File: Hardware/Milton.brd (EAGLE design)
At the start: 53 x 44.8 mm, 83 parts, among them Q1 12MHz, U1 FT231X, U10 SI4464, U3 USD-SOCKETNEW, U4 DDC113TU-7-F, U5 TPS61200, U6 TCR2EE50,LM, U7 MMA8452Q, U8 MAX31850K, U9 BME280, X1 B4B-ZR, X2 M023.5MM, X3 SMA003.062

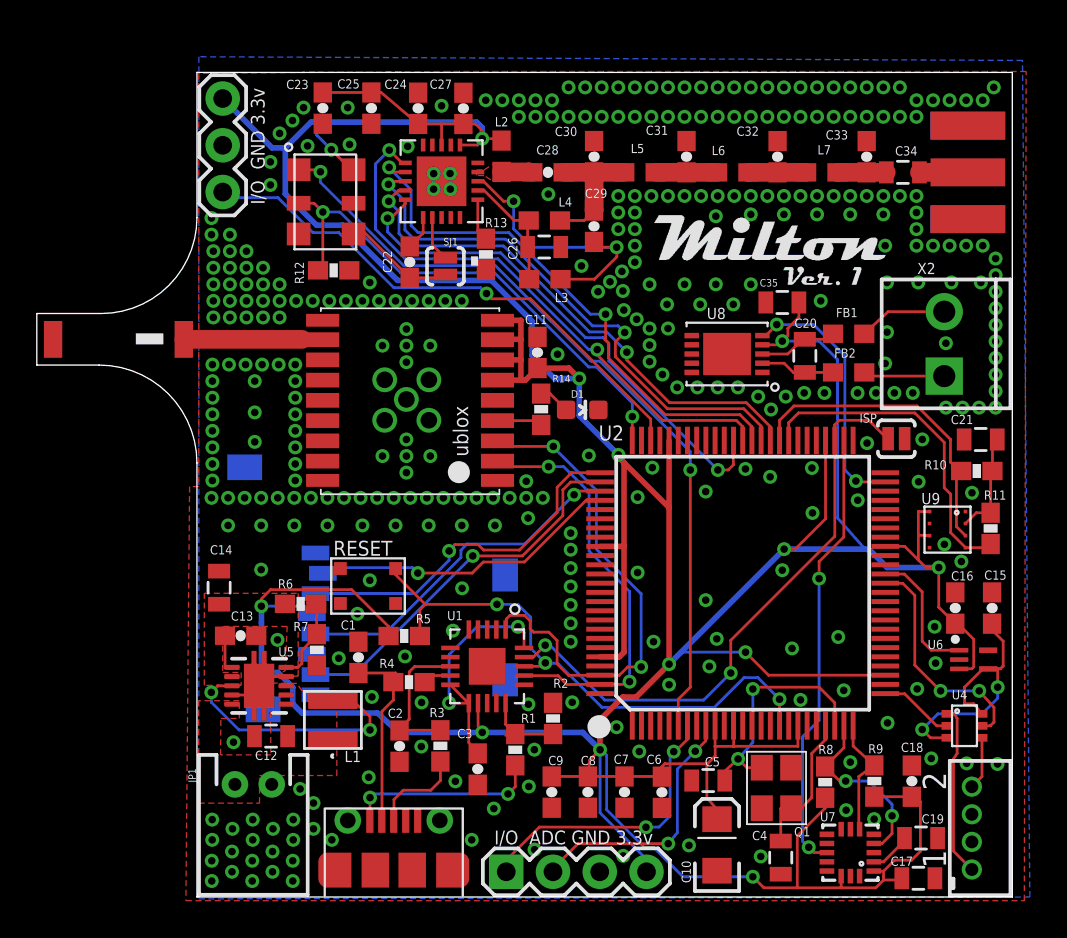
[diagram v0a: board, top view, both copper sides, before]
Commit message: Update
Removed FTDI from board. Added tx/rx header and isp button

Adjusted gps antenna position
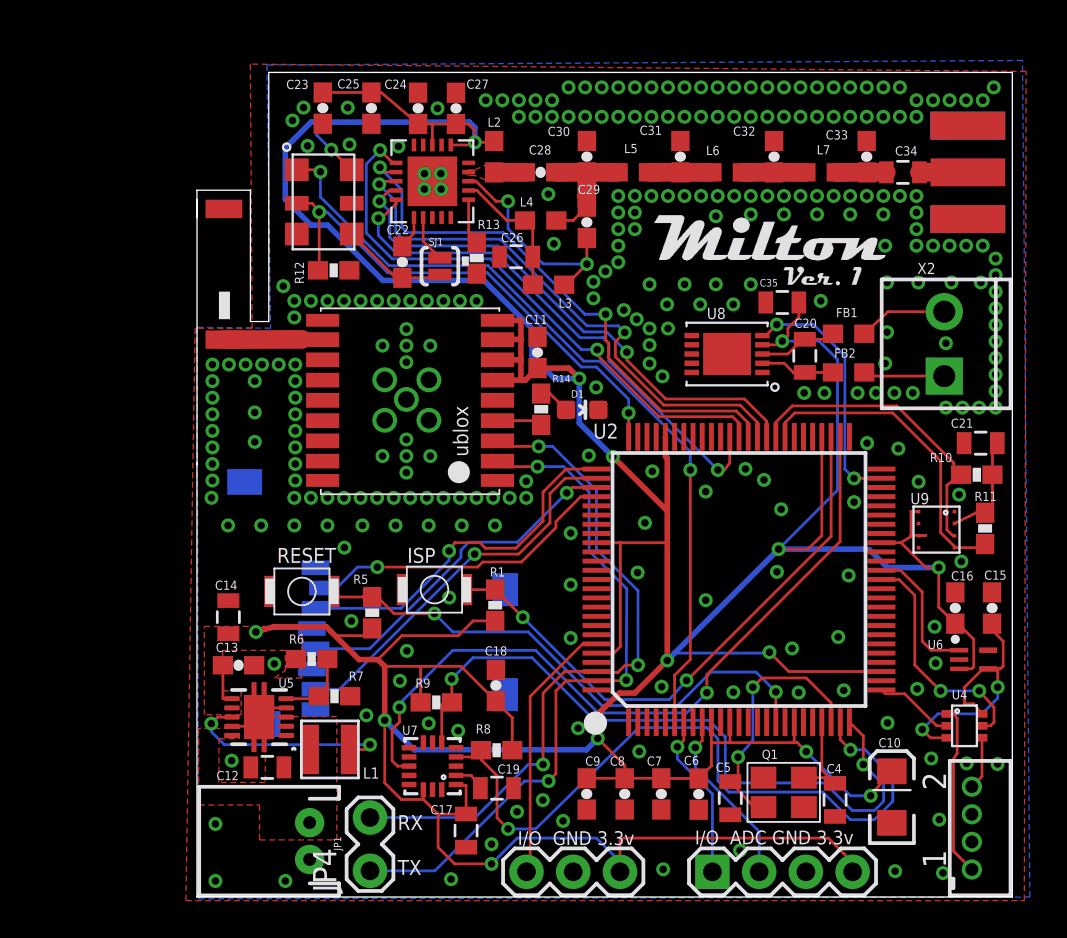
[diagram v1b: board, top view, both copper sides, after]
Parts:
- removed C1, C2: 47pF, SparkFun-Capacitors:0603-CAP
- removed C3: 0.1uF, SparkFun-Capacitors:0603-CAP
- removed R2: 10k, SparkFun-Resistors:0603-RES
- removed R3, R4: 27, SparkFun-Resistors:0603-RES
- removed U$1: USB-MICRO_105017-0001, wrea:USB-MICRO-MOLEX-105017-0001
- removed U1: FT231X, wrea:FT231XQ-R
- added JP4: (no value), SparkFun-Connectors:1X02_LOCK
- ISP: value JUMPER-PAD-2-NOYES_SILK -> SPST.B3U-1000P(M); device SparkFun-Passives:PAD-JUMPER-2-NO_YES_SILK -> omron:B3U-1000P(M)
- JP1: value M02JST-PTH-2 -> (none)
- R1: value 4.7k -> 10K
- RESET: value SWITCH -> SPST.B3U-1000P(M); device notes-arducorder-mini:KMT071 -> omron:B3U-1000P(M)
- moved JP2 40.4 mm to (17.9, 1.37), turned to 0 degrees
- moved ISP 26.4 mm to (12.9, 16.7), turned to 0 degrees
- moved C17 24.7 mm to (14.6, 3.61), turned to 270 degrees
- moved R9 24.2 mm to (13.0, 10.6), turned to 180 degrees
- moved C19 23.2 mm to (16.3, 5.91)
- moved C18 23.2 mm to (16.2, 11.5)
- moved U7 23.2 mm to (12.8, 7.11)
- moved R8 17.9 mm to (16.3, 7.97), turned to 0 degrees
- moved JP3 11.2 mm to (28.0, 1.37)
- moved C10 9.85 mm to (37.8, 5.43)
- moved R1 7.93 mm to (16.2, 15.8)
- moved U$2 6.22 mm to (1.46, 33.5), turned to 90 degrees
- moved JP1 4.34 mm to (6.12, 3.04), turned to 90 degrees
- moved C4 4.30 mm to (34.7, 5.28)
- moved RESET 3.60 mm to (5.70, 16.6), turned to 0 degrees
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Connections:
- removed net N$10: R1.2, U$1.1
- removed net N$12: C3.1, U1.3V3OUT, U1.RESET#, U1.VCCIO
- removed net N$21: R1.1, R2.2, U1.CBUS0
- removed net N$4: C2.1, R3.2, U1.USBDP
- removed net N$5: R4.2, U1.USBDM
- removed net N$7: R3.1, U$1.3
- removed net N$9: C1.2, R4.1, U$1.2
- net 3.3V: now also R1.2; no longer U1.VCC
- net DIGITAL_1: now also U2.95; no longer U2.73
- net GND: now also RESET.1; no longer C1.1, C2.2, C3.2, R2.1, RESET.1A, U$1.5, U1.GND_PIN13, U1.GND_PIN21, U1.GND_PIN3
- net ISP_BOOT: now also R1.1; no longer U1.RTS#
- net RESET: now also RESET.2; no longer RESET.2A, U1.DTR#
- net RXD0: now also JP4.1; no longer U1.TXD
- net TXD0: now also JP4.2; no longer U1.RXD
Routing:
- net SDA0: track 6.57 -> 37.8 mm, vias 0 -> 2
- net SCL0: track 9.92 -> 39.5 mm
- net EINT1: track 24.3 -> 41.0 mm
- net DIGITAL_1: track 29.5 -> 14.4 mm, vias 1 -> 0
- net RXD0: track 23.0 -> 37.7 mm, vias 2 -> 3
- net N$12: track 13.7 -> 0.00 mm, vias 2 -> 0
- net N$9: track 11.2 -> 0.00 mm
- net N$10: track 10.5 -> 0.00 mm, vias 2 -> 0
- net TXD0: track 27.8 -> 37.3 mm, vias 2 -> 3
- net N$4: track 7.95 -> 0.00 mm
- net DIGITAL_2: track 15.9 -> 9.06 mm, vias 2 -> 1
- net N$7: track 5.13 -> 0.00 mm
- net 3.3V: track 290.3 -> 295.2 mm, vias 13 -> 15
- net ADC_IN1: track 14.2 -> 9.72 mm, vias 2 -> 1
- net N$21: track 4.48 -> 0.00 mm
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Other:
- board size 53 x 44.8 mm -> 44.3 x 44.8 mm
- board text added: "RX TX"

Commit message: Cleanup
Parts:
- added U$1: (no value), SparkFun-Aesthetics:OSHW-LOGO-S
- moved R1 4.54 mm to (12.2, 13.8), turned to 180 degrees
- moved L3 0.84 mm to (19.1, 34.1), turned to 270 degrees
- moved C26 0.75 mm to (17.2, 34.1), turned to 90 degrees
- moved ISP 0.70 mm to (12.2, 16.7)
- moved R9 0.67 mm to (13.2, 11.2), turned to 90 degrees
- moved D1 0.63 mm to (20.4, 26.2), turned to 180 degrees
- moved R5 0.60 mm to (8.92, 15.4)
- moved C18 0.51 mm to (16.1, 11.0)
- moved C24 0.43 mm to (11.6, 42.9)
- moved C17 0.43 mm to (14.5, 4.02), turned to 0 degrees
- moved U$4 0.41 mm to (6.47, 37.7)
- moved C25 0.40 mm to (9.07, 42.9)
- moved C23 0.30 mm to (6.53, 42.9)
- moved R12 0.20 mm to (7.43, 33.8)
- moved U7 0.20 mm to (12.6, 7.11)
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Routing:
- net 3.3V: track 295.2 -> 290.4 mm, vias 15 -> 14
- net ISP_BOOT: track 31.4 -> 35.6 mm
- net IC6_RTC2: track 14.2 -> 11.1 mm
- net SDA0: track 37.8 -> 36.1 mm
- net SCL0: track 39.5 -> 38.4 mm
- net RADIO_SEL: track 29.0 -> 28.0 mm
- net N$20: track 12.3 -> 13.2 mm
- net EINT1: track 41.0 -> 40.3 mm
- net RESET: track 30.1 -> 29.4 mm
- net XTAL_EN: track 28.1 -> 28.7 mm
- net GND: vias 285 -> 269
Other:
- board text added: "- +"
